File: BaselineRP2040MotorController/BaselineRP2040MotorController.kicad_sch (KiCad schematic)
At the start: 1 part, among them J4 XT60 Power Connector

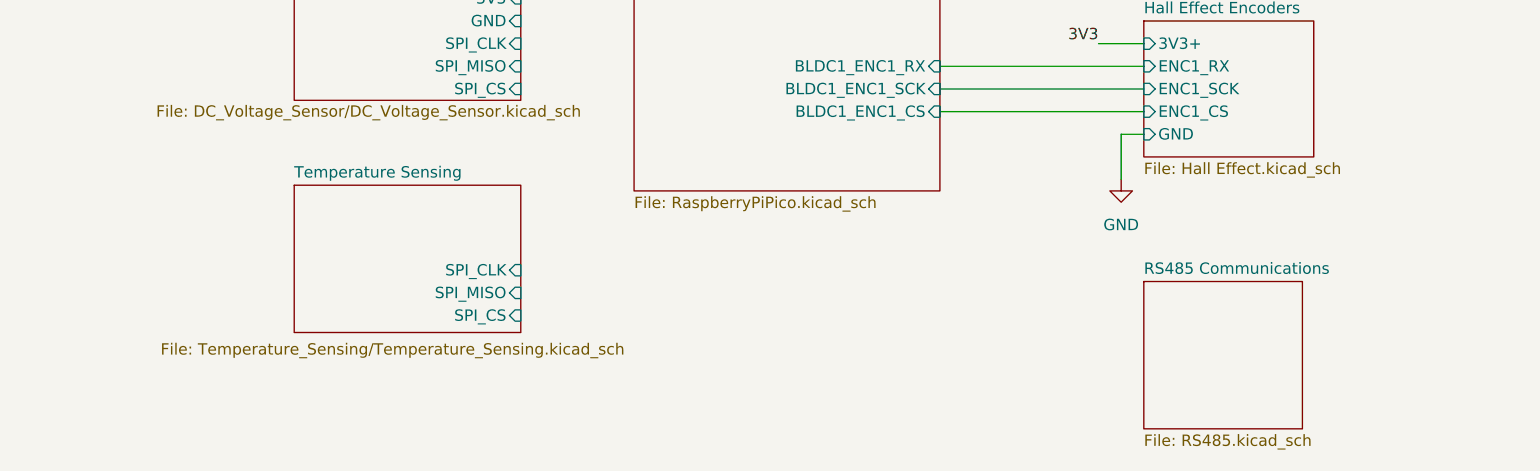
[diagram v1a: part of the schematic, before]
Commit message: Drop some features.
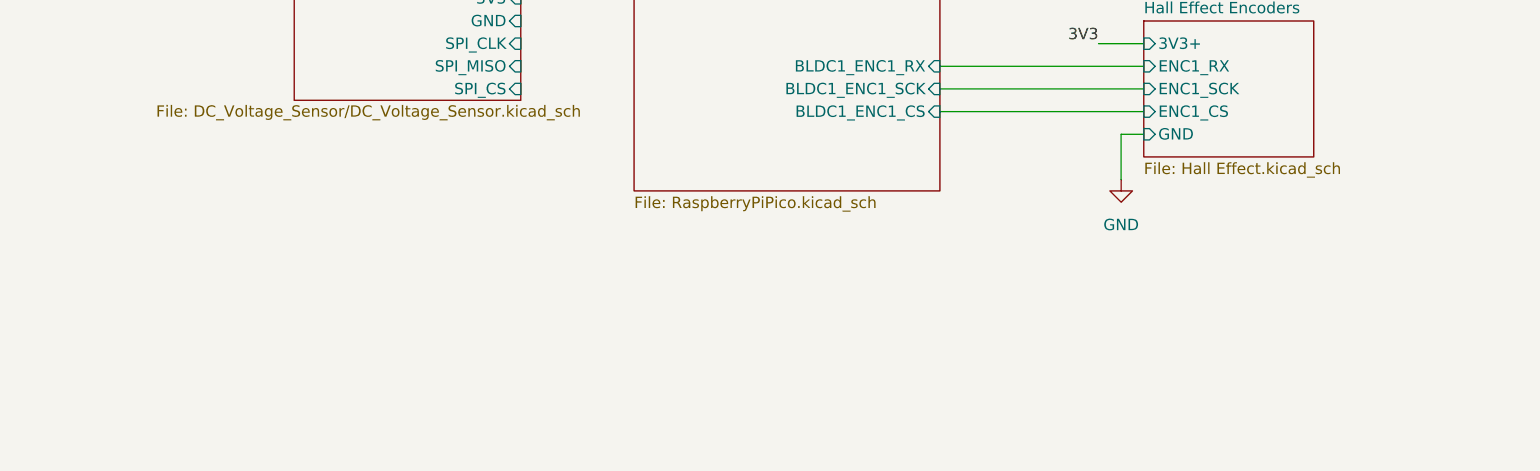
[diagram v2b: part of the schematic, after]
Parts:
- J4: footprint parts:AMASS_XT60PW-F_1x02_P7.20mm_Horizontal -> [EastMakes] Connectors:CONN-TH_XT60UPB-M
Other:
- removed sheet RS485 Communications
- removed sheet Temperature Sensing
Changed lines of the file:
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@@
 			)
 		)
-		(property "Footprint" "parts:AMASS_XT60PW-F_1x02_P7.20mm_Horizontal"
+		(property "Footprint" "[EastMakes] Connectors:CONN-TH_XT60UPB-M"
 			(at 57.15 78.74 0)
 			(effects
@@
 					(reference "J4")
 					(unit 1)
-				)
-			)
-		)
-	)
-	(sheet
-		(at 175.26 142.24)
-		(size 17.78 16.51)
-		(fields_autoplaced yes)
-		(stroke
-			(width 0.1524)
-			(type solid)
-		)
-		(fill
-			(color 0 0 0 0.0000)
-		)
-		(property "Sheetname" "RS485 Communications"
-			(at 175.26 141.5284 0)
-			(effects
-				(font
-					(size 1.27 1.27)
-				)
-				(justify left bottom)
-			)
-		)
-		(property "Sheetfile" "RS485.kicad_sch"
-			(at 175.26 159.3346 0)
-			(effects
-				(font
-					(size 1.27 1.27)
-				)
-				(justify left top)
-			)
-		)
-		(instances
-			(project "BaselineRP2040MotorController"
-				(path "/085e5f08-c826-4caa-b8e2-0a741609456e"
-					(page "9")
 				)
 			)
@@
 				)
 			)
-		)
-	)
-	(sheet
-		(at 80.01 131.445)
-		(size 25.4 16.51)
-		(stroke
-			(width 0.1524)
-			(type solid)
-		)
-		(fill
-			(color 0 0 0 0.0000)
-		)
-		(property "Sheetname" "Temperature Sensing"
-			(at 80.01 130.7334 0)
-			(effects
-				(font
-					(size 1.27 1.27)
-				)
-				(justify left bottom)
-			)
-		)
-		(property "Sheetfile" "Temperature_Sensing/Temperature_Sensing.kicad_sch"
-			(at 65.024 149.098 0)
-			(effects
-				(font
-					(size 1.27 1.27)
-				)
-				(justify left top)
-			)
-		)
-		(pin "SPI_CLK" input
-			(at 105.41 140.97 0)
-			(effects
-				(font
-					(size 1.27 1.27)
-				)
-				(justify right)
-			)
-		)
-		(pin "SPI_MISO" input
-			(at 105.41 143.51 0)
-			(effects
-				(font
-					(size 1.27 1.27)
-				)
-				(justify right)
-			)
-		)
-		(pin "SPI_CS" input
-			(at 105.41 146.05 0)
-			(effects
-				(font
-					(size 1.27 1.27)
-				)
-				(justify right)
-			)
-		)
-		(instances
-			(project "BaselineRP2040MotorController"
-				(path "/085e5f08-c826-4caa-b8e2-0a741609456e"
-					(page "11")
-				)
-			)

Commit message: Just before dropping the self build of the 2040
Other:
- removed sheet Voltage Sensing
- sheet BLDC Power Control ports: added none; removed X_SENSE
- sheet RaspberryPiPico ports: added 5V+; removed none
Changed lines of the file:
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@@
-		)
-	)
-	(wire
-		(pts
-			(xy 80.01 109.22) (xy 77.47 109.22)
-		)
-		(stroke
-			(width 0)
-			(type default)
 		)
 	)
@@
 		(pts
 			(xy 152.4 96.52) (xy 175.26 96.52)
+		)
+		(stroke
+			(width 0)
+			(type default)
+		)
+	)
+	(wire
+		(pts
+			(xy 118.11 82.55) (xy 116.84 82.55)
 		)
 		(stroke
@@
 		)
 	)
+	(label "5V"
+		(at 116.84 82.55 180)
+		(fields_autoplaced yes)
+		(effects
+			(font
+				(size 1.27 1.27)
+			)
+			(justify right bottom)
+		)
+	)
 	(label "3V3"
 		(at 116.84 86.36 180)
@@
 			)
 			(justify left bottom)
-		)
-	)
-	(label "VMOT"
-		(at 77.47 109.22 180)
-		(fields_autoplaced yes)
-		(effects
-			(font
-				(size 1.27 1.27)
-			)
-			(justify right bottom)
 		)
 	)
@@
 	)
 	(sheet
-		(at 80.01 105.41)
-		(size 25.4 16.51)
+		(at 175.26 113.03)
+		(size 19.05 15.24)
+		(fields_autoplaced yes)
 		(stroke
 			(width 0.1524)
@@
 			(color 0 0 0 0.0000)
 		)
-		(property "Sheetname" "Voltage Sensing"
-			(at 80.01 104.6984 0)
-			(effects
-				(font
-					(size 1.27 1.27)
-				)
-				(justify left bottom)
-			)
-		)
-		(property "Sheetfile" "DC_Voltage_Sensor/DC_Voltage_Sensor.kicad_sch"
-			(at 64.516 122.428 0)
-			(effects
-				(font
-					(size 1.27 1.27)
-				)
-				(justify left top)
-			)
-		)
-		(pin "3V3" input
-			(at 105.41 110.49 0)
-			(effects
-				(font
-					(size 1.27 1.27)
-				)
-				(justify right)
-			)
-		)
-		(pin "GND" input
-			(at 105.41 113.03 0)
-			(effects
-				(font
-					(size 1.27 1.27)
-				)
-				(justify right)
-			)
-		)
-		(pin "VMOT_PWR" input
-			(at 80.01 109.22 180)
-			(effects
-				(font
-					(size 1.27 1.27)
-				)
-				(justify left)
-			)
-		)
-		(pin "SPI_CLK" input
-			(at 105.41 115.57 0)
-			(effects
-				(font
-					(size 1.27 1.27)
-				)
-				(justify right)
-			)
-		)
-		(pin "SPI_CS" input
-			(at 105.41 120.65 0)
-			(effects
-				(font
-					(size 1.27 1.27)
-				)
-				(justify right)
-			)
-		)
-		(pin "SPI_MISO" input
-			(at 105.41 118.11 0)
-			(effects
-				(font
-					(size 1.27 1.27)
-				)
-				(justify right)
-			)
-		)
-		(instances
-			(project "BaselineRP2040MotorController"
-				(path "/085e5f08-c826-4caa-b8e2-0a741609456e"
-					(page "10")
-				)
-			)
-		)
-	)
-	(sheet
-		(at 175.26 113.03)
-		(size 19.05 15.24)
-		(fields_autoplaced yes)
-		(stroke
-			(width 0.1524)
-			(type solid)
-		)
-		(fill
-			(color 0 0 0 0.0000)
-		)
 		(property "Sheetname" "Hall Effect Encoders"
 			(at 175.26 112.3184 0)
@@
 			)
 		)
-		(pin "GND" input
+		(pin "GND" bidirectional
 			(at 175.26 125.73 180)
 			(effects
@@
 			)
 		)
-		(pin "GND" input
+		(pin "GND" bidirectional
 			(at 80.01 95.25 180)
 			(effects
@@
 			)
 		)
-		(pin "X_SENSE" output
-			(at 175.26 102.87 180)
-			(effects
-				(font
-					(size 1.27 1.27)
-				)
-				(justify left)
-			)
-		)
 		(pin "U_SENSE" output
 			(at 175.26 105.41 180)
@@
 			)
 		)
-		(pin "GND" input
+		(pin "GND" bidirectional
 			(at 118.11 90.17 180)
 			(effects
@@
 			)
 		)
+		(pin "5V+" input
+			(at 118.11 82.55 180)
+			(effects
+				(font
+					(size 1.27 1.27)
+				)
+				(justify left)
+			)
+		)

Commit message: Erhhhhrh
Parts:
- added U1: Pico, [EastMakes] PiPico:RPi_Pico_SMD_TH, symbol [EastMakes] PiPico:Pico
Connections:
- net BLDC Power Control/PWM_H_U: now also U1.6 (GPIO4)
- net BLDC Power Control/PWM_H_V: now also U1.9 (GPIO6)
- net BLDC Power Control/PWM_H_X: now also U1.11 (GPIO8)
- net BLDC Power Control/PWM_L_U: now also U1.7 (GPIO5)
- net BLDC Power Control/PWM_L_V: now also U1.10 (GPIO7)
- net BLDC Power Control/PWM_L_X: now also U1.12 (GPIO9)
- new net CurrentSense1: U1.31 (GPIO26_ADC0)
- new net CurrentSense2: U1.32 (GPIO27_ADC1)
- new net Encoder CS: U1.26 (GPIO20)
- new net Encoder RX: U1.29 (GPIO22)
- new net Encoder SCK: U1.27 (GPIO21)
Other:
- removed sheet RaspberryPiPico
- sheet Power Filtering ports: added none; removed 3V3+, 5V+
- moved on the sheet: J4

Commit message: Going to take a break.
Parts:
- removed U1: Pico, [EastMakes] PiPico:RPi_Pico_SMD_TH, symbol [EastMakes] PiPico:Pico
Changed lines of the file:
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@@
-	)
-	(symbol
-		(lib_id "[EastMakes] PiPico:Pico")
-		(at 129.54 95.25 0)
-		(mirror y)
-		(unit 1)
-		(exclude_from_sim no)
-		(in_bom yes)
-		(on_board yes)
-		(dnp no)
-		(property "Reference" "U1"
-			(at 129.54 63.5 0)
-			(effects
-				(font
-					(size 1.27 1.27)
-				)
-			)
-		)
-		(property "Value" "Pico"
-			(at 129.54 66.04 0)
-			(effects
-				(font
-					(size 1.27 1.27)
-				)
-			)
-		)
-		(property "Footprint" "[EastMakes] PiPico:RPi_Pico_SMD_TH"
-			(at 129.54 95.25 90)
-			(effects
-				(font
-					(size 1.27 1.27)
-				)
-				(hide yes)
-			)
-		)
-		(property "Datasheet" ""
-			(at 129.54 95.25 0)
-			(effects
-				(font
-					(size 1.27 1.27)
-				)
-				(hide yes)
-			)
-		)
-		(property "Description" ""
-			(at 129.54 95.25 0)
-			(effects
-				(font
-					(size 1.27 1.27)
-				)
-				(hide yes)
-			)
-		)
-		(pin "7"
-		)
-		(pin "16"
-		)
-		(pin "41"
-		)
-		(pin "18"
-		)
-		(pin "19"
-		)
-		(pin "22"
-		)
-		(pin "15"
-		)
-		(pin "23"
-		)
-		(pin "26"
-		)
-		(pin "20"
-		)
-		(pin "24"
-		)
-		(pin "29"
-		)
-		(pin "3"
-		)
-		(pin "31"
-		)
-		(pin "33"
-		)
-		(pin "34"
-		)
-		(pin "10"
-		)
-		(pin "17"
-		)
-		(pin "35"
-		)
-		(pin "36"
-		)
-		(pin "4"
-		)
-		(pin "42"
-		)
-		(pin "5"
-		)
-		(pin "6"
-		)
-		(pin "30"
-		)
-		(pin "1"
-		)
-		(pin "12"
-		)
-		(pin "40"
-		)
-		(pin "9"
-		)
-		(pin "13"
-		)
-		(pin "32"
-		)
-		(pin "8"
-		)
-		(pin "38"
-		)
-		(pin "21"
-		)
-		(pin "14"
-		)
-		(pin "28"
-		)
-		(pin "43"
-		)
-		(pin "2"
-		)
-		(pin "27"
-		)
-		(pin "39"
-		)
-		(pin "25"
-		)
-		(pin "37"
-		)
-		(pin "11"
-		)
-		(instances
-			(project "BaselineRP2040MotorController"
-				(path "/085e5f08-c826-4caa-b8e2-0a741609456e"
-					(reference "U1")
-					(unit 1)
-				)
-			)
-		)
 	)
 	(symbol

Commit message: Release for Review
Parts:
- added J1: To UC, symbol Connector_Generic:Conn_02x08_Counter_Clockwise
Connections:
- net 3V3: now also J1.16 (Pin_16), J1.9 (Pin_9)
- net CurrentSense1: now also J1.12 (Pin_12)
- net CurrentSense2: now also J1.5 (Pin_5)
- net Encoder CS: now also J1.10 (Pin_10)
- net Encoder RX: now also J1.6 (Pin_6)
- net Encoder SCK: now also J1.7 (Pin_7)
- net GND: now also J1.1 (Pin_1), J1.8 (Pin_8)
- new net CurrentSense3: J1.11 (Pin_11)
- new net PWM L U: J1.2 (Pin_2)
- new net PWM L V: J1.3 (Pin_3)
- new net PWM L X: J1.4 (Pin_4)
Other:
- sheet BLDC Power Control ports: added X_SENSE; removed none
- note removed: "RP2040"
- note removed: "Regulated 3.3V Output"

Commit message: Generate PDF
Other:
- title: (none) -> BLDC Starting Point
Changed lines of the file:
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@@
 	(generator_version "8.0")
 	(paper "A4")
+	(title_block
+		(title "BLDC Starting Point")
+		(comment 1 "Florian, Josh and EMF Group Release")
+	)
 	(junction
 		(at 46.99 78.74)

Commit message: Post Feedback Changes.
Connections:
- net 12V: now also J1.9 (Pin_9)
- net 3V3: no longer J1.9 (Pin_9)
- net Power Filtering/VMOT_RAW renamed VMOT_RAW
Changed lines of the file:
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@@
+		)
+	)
+	(label "VMOT_RAW"
+		(at 168.91 76.2 180)
+		(fields_autoplaced yes)
+		(effects
+			(font
+				(size 1.27 1.27)
+			)
+			(justify right bottom)
 		)
 	)
@@
 		)
 	)
+	(label "VMOT_RAW"
+		(at 50.8 76.2 0)
+		(fields_autoplaced yes)
+		(effects
+			(font
+				(size 1.27 1.27)
+			)
+			(justify left bottom)
+		)
+	)
 	(label "3V3"
 		(at 137.16 78.74 0)
@@
 		)
 	)
-	(label "3V3"
+	(label "12V"
 		(at 137.16 96.52 0)
 		(fields_autoplaced yes)
@@
 		(fields_autoplaced yes)
 		(effects
-			(font
-				(size 1.27 1.27)
-			)
-			(justify right bottom)
-		)
-	)
-	(label "VMOT"
-		(at 168.91 76.2 180)
-		(fields_autoplaced yes)
-		(effects
